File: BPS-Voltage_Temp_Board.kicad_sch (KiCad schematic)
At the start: 2 parts, among them U2 BQ7692003PW, U3 PeripheralSOM

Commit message: rough layout done -connectors are not fully chosen yet, nano for temp, ??? for volt taps
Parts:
- added C10, C11, C12, C13, C4, C7, C9: 1μF, Capacitor_SMD:C_0805_2012Metric, symbol Device:C_Small
- added C5: 4.7μF, Capacitor_SMD:C_0805_2012Metric, symbol Device:C_Small
- added C6: 4.7pF, Capacitor_SMD:C_0805_2012Metric, symbol Device:C_Small
- added C8: 10μF, Capacitor_SMD:C_0805_2012Metric, symbol Device:C_Small
- added J2: voltage taps, Connector_Molex:Molex_Micro-Fit_3.0_43650-0915_1x09_P3.00mm_Vertical, symbol Connector_Generic:Conn_01x09
- added J4, J5: I-CanConn, Connector_Molex:Molex_Micro-Fit_3.0_43650-0415_1x04_P3.00mm_Vertical, symbol Connector_Generic:Conn_01x04
- added Q1: mmftp3334k, Package_TO_SOT_SMD:SOT-23, symbol Simulation_SPICE:PMOS
- added R10, R4, R5, R6, R7, R9: 100Ω, Resistor_SMD:R_0805_2012Metric, symbol Device:R
- added R11: 2kΩ, Resistor_SMD:R_0805_2012Metric, symbol Device:R
- added R12, R13, R8: 10kΩ, Resistor_SMD:R_0805_2012Metric, symbol Device:R
- added R14: 100kΩ, Resistor_SMD:R_0805_2012Metric, symbol Device:R
- added R15: 0Ω, Resistor_SMD:R_0805_2012Metric, symbol Device:R
- added R3: 500kΩ, Resistor_SMD:R_0805_2012Metric, symbol Device:R
- added SW1: BMS_BOOT, Button_Switch_SMD:SW_SPST_B3SL-1002P, symbol Switch:SW_Push
- added U4: ISO1641BDR, footprints:SOIC8_D_TEX, symbol ISO1541QDQ1:ISO1641BDR
- added U5, U6: EL3H7, Package_SO:SSOP-4_4.4x2.6mm_P1.27mm, symbol Isolator:SFH617A-1
- U2: footprint PW0020A_N -> footprints:PW0020A_N
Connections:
- net +12V: now also J4.1 (Pin_1), J5.1 (Pin_1)
- net +3.3V: now also U4.1 (VCC1), U6.4
- net GND: now also R12.1, U4.4 (GND1), U5.2
- net GNDPWR: now also J4.4 (Pin_4), J5.4 (Pin_4)
- net bmSCL: now also U4.6 (SCL2); no longer U3.14 (I2C1_SCL)
- net bmSDA: now also U4.7 (SDA2); no longer U3.16 (I2C1_SDA)
- net at U2.10 (BAT): now also C8.2, R4.1
- net VC5: now reaches U2.12 (VC5)
- net VC5: now also R15.1
- net VC4: now reaches U2.13 (VC4)
- net VC4: now also C12.2, R15.2, R9.1
- net VC3: now reaches U2.14 (VC3)
- net VC3: now also C11.2, C12.1, R10.1
- net VC2: now reaches U2.15 (VC2)
- net VC2: now also C10.2, C11.1, R7.1
- net VC1: now reaches U2.16 (VC1)
- net VC1: now also C10.1, C9.2, Q1.3 (S), R14.2, R6.1, SW1.1, U4.8 (VCC2)
- net VC0: now reaches U2.17 (VC0)
- net VC0: now also C13.1, R5.1
- net GND2: now reaches U2.18 (SRP)
- net GND2: now also U2.19 (SRN), U2.3 (VSS), C13.2, C4.1, C5.1, C6.1, C7.1, C8.1, C9.1, J2.1 (Pin_1), R5.2, R8.1, U4.5 (GND2), U5.4, U6.2
- net at U2.20 (ALERT): now also C6.2, R3.1
- net at U2.6 (TS1): now also R13.2, R8.2
- net at U2.7 (CAP1): now also C4.2
- net at U2.8 (REGOUT): now also C5.2
- net cell4+: now reaches U2.9 (REGSRC)
- net cell4+: now also C7.2, J2.9 (Pin_9), R4.2, R9.2
- net I-CAN_L: now reaches U3.21 (CAN_L)
- net I-CAN_L: now also J4.3 (Pin_3), J5.3 (Pin_3)
- net I-CAN_H: now reaches U3.23 (CAN_H)
- net I-CAN_H: now also J4.2 (Pin_2), J5.2 (Pin_2)
- net bmsEN: now reaches U3.5 (SPI2_SCK)
- net bmsEN: now also R11.1
- net bmsALERT: now reaches U3.7 (SPI2_NSS)
- net bmsALERT: now also R12.2, U6.3
- new net: R3.2, U6.1
- new net: R11.2, U5.1
- new net: Q1.2 (G), R14.1, U5.3
- new net: Q1.1 (D), R13.1, SW1.2
- new net 1&2COM: J2.3 (Pin_3), R6.2
- new net 2&3COM: J2.5 (Pin_5), R7.2
- new net 3&4COM: J2.7 (Pin_7), R10.2
- new net psSCL: U3.14 (I2C1_SCL), U4.3 (SCL1)
- new net psSDA: U3.16 (I2C1_SDA), U4.2 (SDA1)
- no-connect marks 6 -> 11
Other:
- note added: "BMS Chip & Octocouplers"
- note added: "I2C Isolator"
- note added: "Psom & ICAN Connectors"
- note added: "Thermistor Town"
- note added: "Voltage taps & caps"
- note added: "pull alert low"
- note added: "pull p-mos high"
- note added: "pull ts1 down to vss"
- note added: "short last pin"
- note added: "vertical conn"
- moved on the sheet: U2

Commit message: Addressed some concerns
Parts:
- added D1: D_Zener_Small, symbol Device:D_Zener_Small
- added F1, F10, F2, F3, F4, F5, F6, F7, F8, F9: 10mA, UTSVT_Special:ptc_fuse_FUSC1607X75N, symbol Device:Polyfuse_Small
- added J1: bms i2c test, symbol Connector:Conn_01x02_Pin
- added R22, R23: 100kΩ, Resistor_SMD:R_0805_2012Metric, symbol Device:R
- added R24, R25: 1kΩ, Resistor_SMD:R_0805_2012Metric, symbol Device:R
- added SW2: SW_DIP_x05, symbol Switch:SW_DIP_x05
- added TP10: cellgndinject, symbol Connector:TestPoint_Small
- added TP11: 1&2inject, symbol Connector:TestPoint_Small
- added TP12: 2&3inject, symbol Connector:TestPoint_Small
- added TP13: 3&4inject, symbol Connector:TestPoint_Small
- added TP14: cell4inject, symbol Connector:TestPoint_Small
- added TP17: regout testpoint, symbol Connector:TestPoint_Small
- added TP18: bmsAlert test, symbol Connector:TestPoint_Small
- added TP19: bmsEN test, symbol Connector:TestPoint_Small
- added TP6: BAT tap, symbol Connector:TestPoint_Small
- added TP7: VSS tap, symbol Connector:TestPoint_Small
- J2: footprint Connector_Molex:Molex_Micro-Fit_3.0_43650-0915_1x09_P3.00mm_Vertical -> Connector_Molex:Molex_Nano-Fit_105314-xx10_2x05_P2.50mm_Horizontal
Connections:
- net 1&2COM: now also F7.2; no longer J2.3 (Pin_3)
- net 2&3COM: now also F8.2; no longer J2.5 (Pin_5)
- net 3&4COM: now also F9.2; no longer J2.7 (Pin_7)
- net GND2: now also R3.2, F6.2, TP7.1; no longer J2.1 (Pin_1)
- net VC1: no longer Q1.3 (S), R14.2, SW1.1, U4.8 (VCC2)
- net VC3: now also R15.1
- net VC4: no longer C12.2, R9.1
- net VC5: now also C12.2, R9.1; no longer R15.1
- net bmSCL: now also J1.2 (Pin_2), R23.1
- net bmSDA: now also J1.1 (Pin_1), R22.1
- net bmsALERT: now also TP18.1
- net bmsEN: now also TP19.1
- net cell4+: now also D1.2 (A), F10.2, R25.2; no longer C7.2, J2.9 (Pin_9), R4.2, U2.9 (REGSRC)
- net at C6.2, R3.1, U2.20 (ALERT): now also U6.1
- net at C8.2, R4.1, U2.10 (BAT): now also TP6.1
- net regout: now reaches C5.2, U2.8 (REGOUT)
- net regout: now also Q1.3 (S), R14.2, SW1.1, U4.8 (VCC2), R22.2, R23.2, TP17.1
- new net: F1.1, SW2.1
- new net: F10.1, SW2.10, TP14.1
- new net: F2.1, SW2.2
- new net: F3.1, SW2.3
- new net: F4.1, SW2.4
- new net: F5.1, SW2.5
- new net: F6.1, SW2.6, TP10.1
- new net: F7.1, SW2.7, TP11.1
- new net: F8.1, SW2.8, TP12.1
- new net: F9.1, SW2.9, TP13.1
- new net: F5.2, J2.1 (Pin_1)
- new net: C7.2, R24.1, U2.9 (REGSRC)
- new net: F2.2, J2.7 (Pin_7)
- new net: F4.2, J2.3 (Pin_3)
- new net: F3.2, J2.5 (Pin_5)
- new net: F1.2, J2.9 (Pin_9)
- new net: D1.1 (K), R24.2, R25.1, R4.2
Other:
- sheet Thermistor town: file untitled.kicad_sch -> ADC_related.kicad_sch
- note added: "I-CAN connectors"
- note added: "Voltage taps & caps (DIP switch for scrutineering)"
- note added: "bat and regsrc connected"
- note added: "short 3&4 - last cell goes to vc5"
- note added: "volt tap antialiasing"
- note removed: "Voltage taps & caps"
- note removed: "short last pin"
- moved on the sheet: C10, C11, C12, C13, C4, C5, C6, C7, C8, C9, J4, J5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

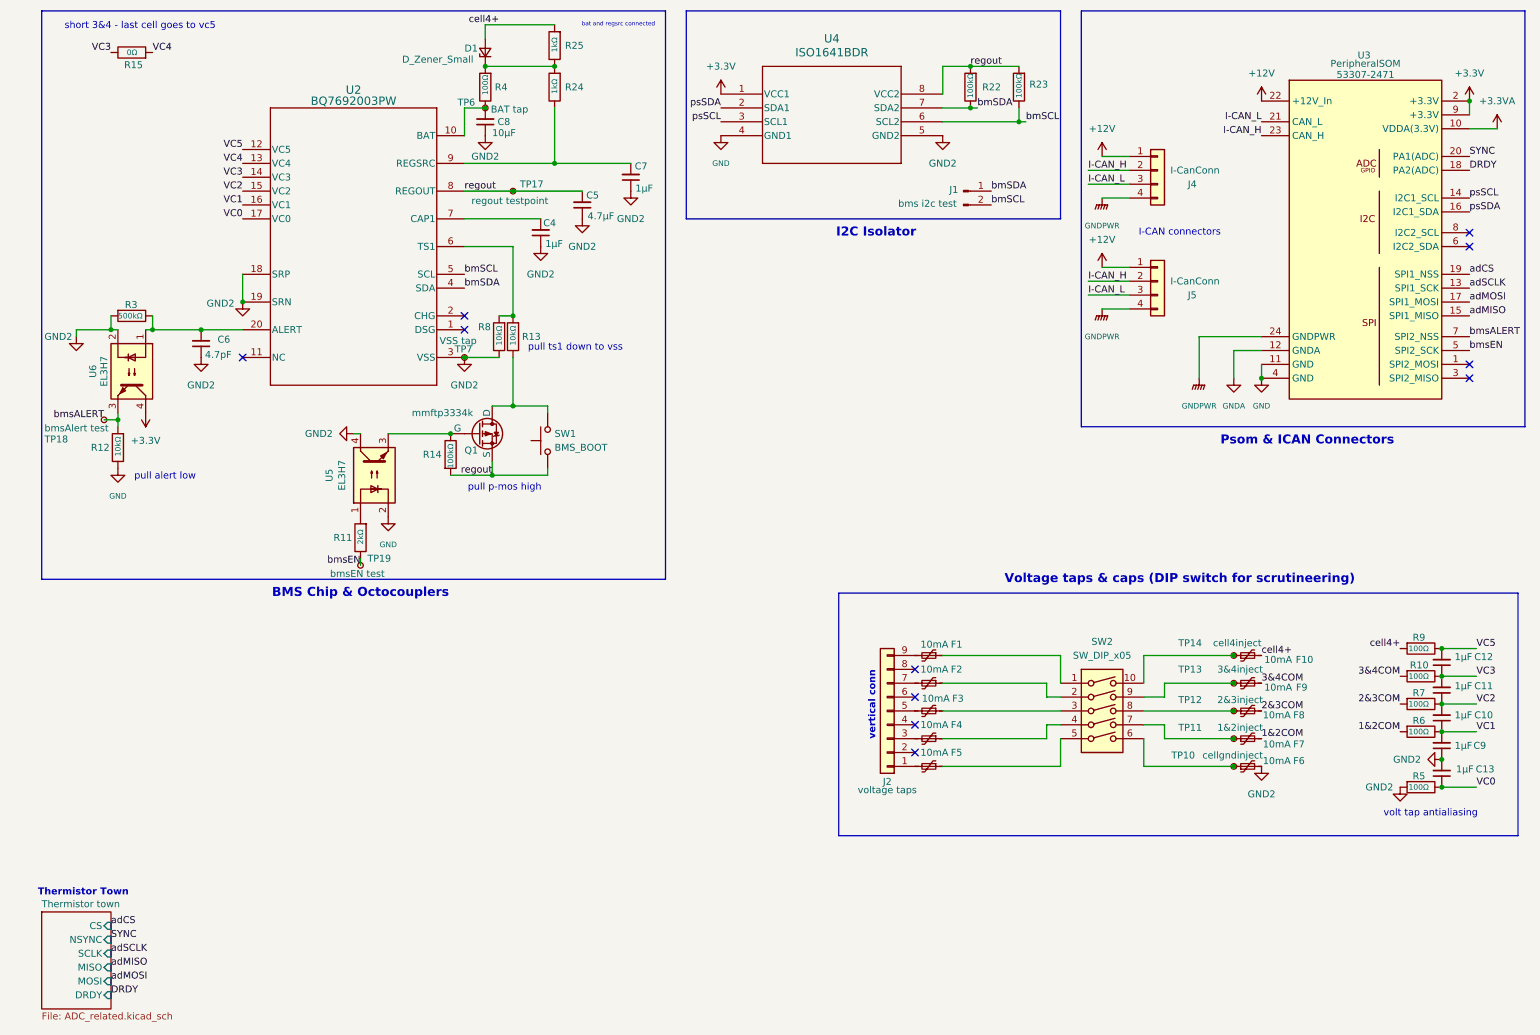
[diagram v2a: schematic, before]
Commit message: Added test points pre DIP. Removed p-mos, per boot switch pdf. Cleaned up symbols.
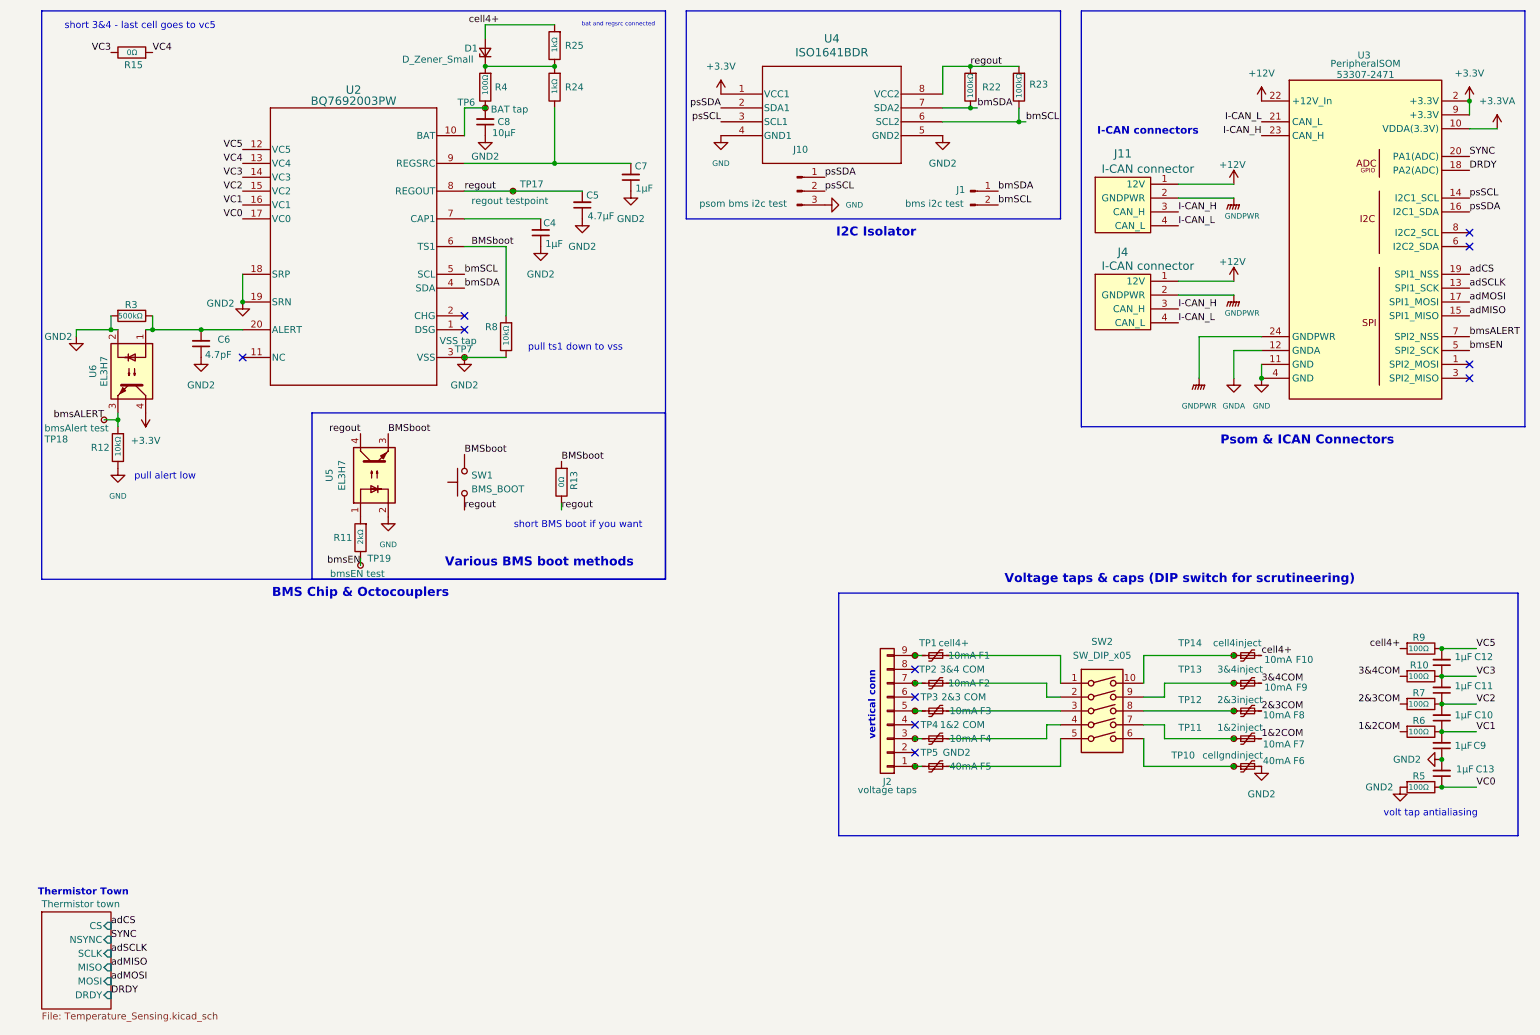
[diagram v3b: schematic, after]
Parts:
- removed J4, J5: I-CanConn, Connector_Molex:Molex_Micro-Fit_3.0_43650-0415_1x04_P3.00mm_Vertical, symbol Connector_Generic:Conn_01x04
- removed Q1: mmftp3334k, Package_TO_SOT_SMD:SOT-23, symbol Simulation_SPICE:PMOS
- removed R14: 100kΩ, Resistor_SMD:R_0805_2012Metric, symbol Device:R
- added J10: psom bms i2c test, symbol Connector:Conn_01x03_Pin
- added J11, J4: I-CAN connector, UTSVT_Connectors:Molex_MicroFit3.0_1x4xP3.00mm_PolarizingPeg_Vertical, symbol utsvt-connectors:PeripheralCANConnector
- added TP1: cell4+, symbol Connector:TestPoint_Small
- added TP2: 3&4 COM, symbol Connector:TestPoint_Small
- added TP3: 2&3 COM, symbol Connector:TestPoint_Small
- added TP4: 1&2 COM, symbol Connector:TestPoint_Small
- added TP5: GND2, symbol Connector:TestPoint_Small
- F5, F6: value 10mA -> 40mA
- R13: value 10kΩ -> 0Ω
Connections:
- net +12V: now also J11.1 (12V), J4.1 (12V)
- net GND: now also J10.3 (Pin_3)
- net GND2: no longer U5.4
- net GNDPWR: now also J11.2 (GNDPWR), J4.2 (GNDPWR)
- net I-CAN_H: now also J11.3 (CAN_H), J4.3 (CAN_H)
- net I-CAN_L: now also J11.4 (CAN_L), J4.4 (CAN_L)
- net psSCL: now also J10.2 (Pin_2)
- net psSDA: now also J10.1 (Pin_1)
- net regout: now also R13.1, U5.4
- net at F5.2, J2.1 (Pin_1): now also TP5.1
- net BMSboot: now reaches U5.3
- net BMSboot: now also R13.2, R8.2, SW1.2, U2.6 (TS1)
- net at F2.2, J2.7 (Pin_7): now also TP2.1
- net at F4.2, J2.3 (Pin_3): now also TP4.1
- net at F3.2, J2.5 (Pin_5): now also TP3.1
- net at F1.2, J2.9 (Pin_9): now also TP1.1
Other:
- sheet Thermistor town: file ADC_related.kicad_sch -> Temperature_Sensing.kicad_sch
- note added: "Various BMS boot methods"
- note added: "short BMS boot if you want"
- note removed: "pull p-mos high"
- moved on the sheet: F1, F2, F3, F4, F5, J1, R8, SW1

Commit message: nothing changedgit add .git add . (do not look at commit history :))
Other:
- title: (none) -> BPS Voltage&Temperature board 
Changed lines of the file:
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@@
 	(generator_version "8.0")
 	(paper "A4")
+	(title_block
+		(title "BPS Voltage&Temperature board ")
+		(date "2025-03-05")
+	)
 	(junction
 		(at 236.22 80.01)
@@
 			)
 		)
-		(property "Datasheet" "ISO1641BDR"
+		(property "Datasheet" "https://www.ti.com/lit/ds/symlink/iso1641.pdf?ts=1741147731751&ref_url=https%253A%252F%252Fwww.ti.com%252Fproduct%252FISO1641%252Fpart-details%252FISO1641BDR"
 			(at 137.16 27.94 0)
 			(effects
